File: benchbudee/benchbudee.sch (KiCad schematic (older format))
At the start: 0 parts

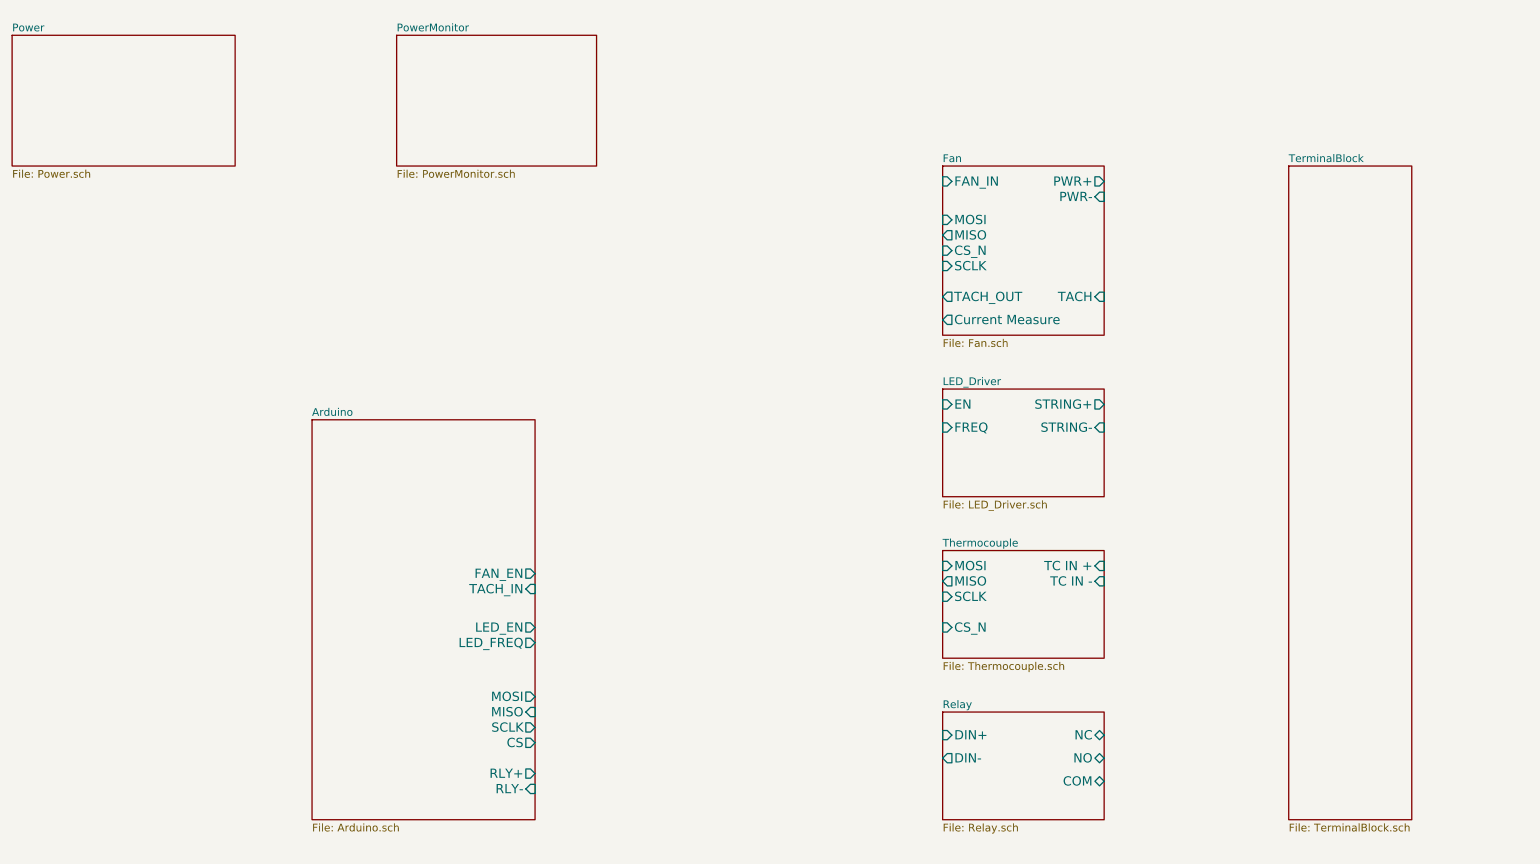
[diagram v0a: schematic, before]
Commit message: Added power monitor module
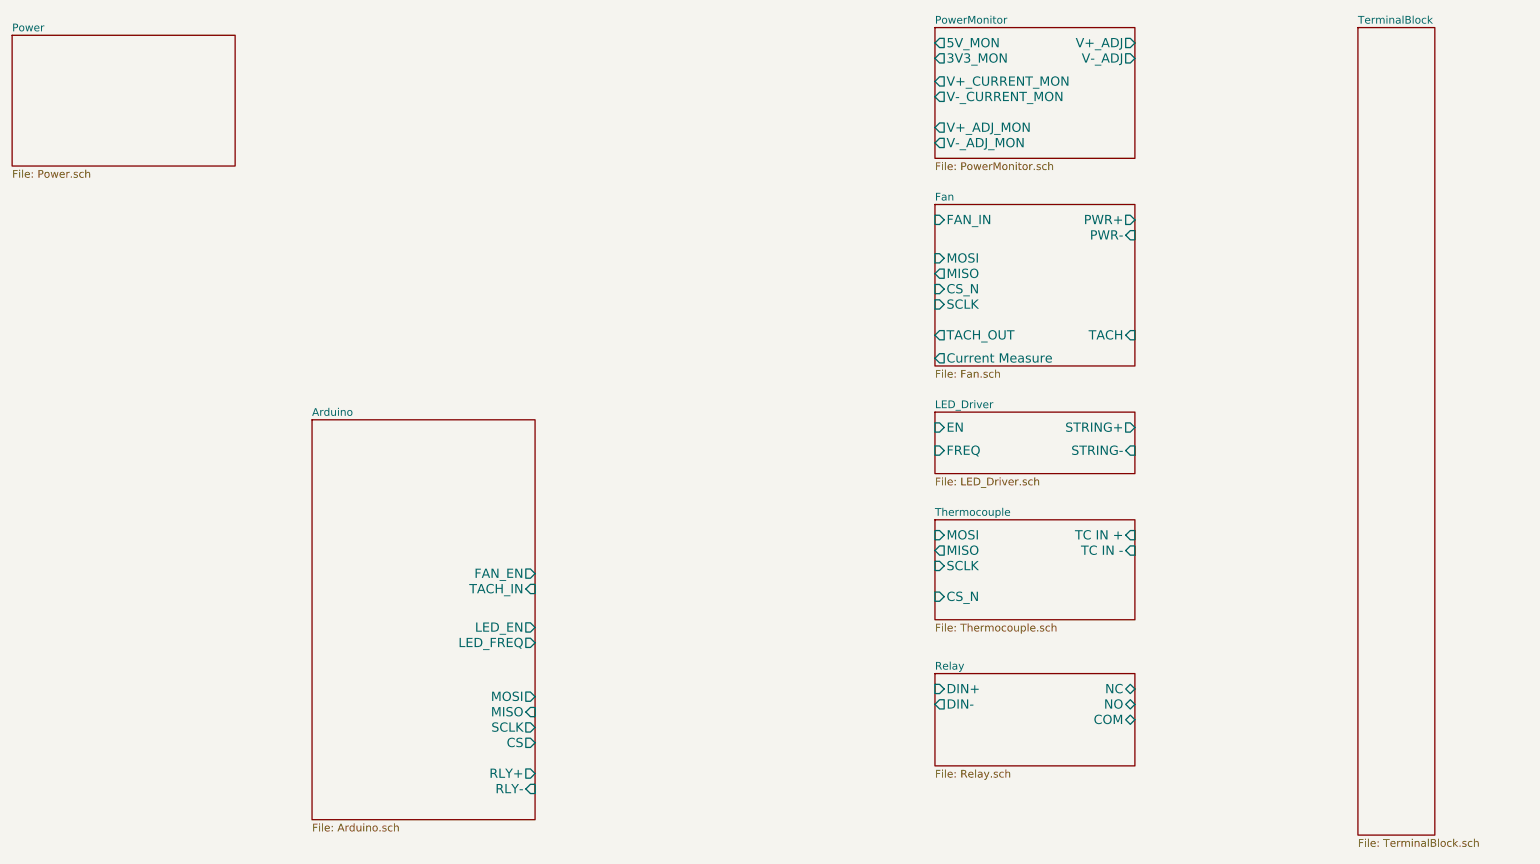
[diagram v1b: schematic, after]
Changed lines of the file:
@@
 Sheet 1 9
 Title ""
-Date "13 feb 2014"
+Date "14 feb 2014"
 Rev ""
 Comp ""
@@
 $EndSheet
 $Sheet
-S 7150 4300 1050 700
+S 7100 4100 1300 650
 U 52F13E8B
 F0 "Thermocouple" 50
 F1 "Thermocouple.sch" 50
-F2 "TC IN +" I R 8200 4400 60
-F3 "TC IN -" I R 8200 4500 60
-F4 "MOSI" I L 7150 4400 60
-F5 "MISO" O L 7150 4500 60
-F6 "SCLK" I L 7150 4600 60
-F7 "CS_N" I L 7150 4800 60
+F2 "TC IN +" I R 8400 4200 60
+F3 "TC IN -" I R 8400 4300 60
+F4 "MOSI" I L 7100 4200 60
+F5 "MISO" O L 7100 4300 60
+F6 "SCLK" I L 7100 4400 60
+F7 "CS_N" I L 7100 4600 60
 $EndSheet
 $Sheet
-S 7150 5350 1050 700
+S 7100 5100 1300 600
 U 52F13E9E
 F0 "Relay" 50
 F1 "Relay.sch" 50
-F2 "DIN+" I L 7150 5500 60
-F3 "DIN-" O L 7150 5650 60
-F4 "NC" B R 8200 5500 60
-F5 "NO" B R 8200 5650 60
-F6 "COM" B R 8200 5800 60
+F2 "DIN+" I L 7100 5200 60
+F3 "DIN-" O L 7100 5300 60
+F4 "NC" B R 8400 5200 60
+F5 "NO" B R 8400 5300 60
+F6 "COM" B R 8400 5400 60
 $EndSheet
 $Sheet
@@
 $EndSheet
 $Sheet
-S 7150 3250 1050 700
+S 7100 3400 1300 400
 U 52F1408A
 F0 "LED_Driver" 50
 F1 "LED_Driver.sch" 50
-F2 "EN" I L 7150 3350 60
-F3 "FREQ" I L 7150 3500 60
-F4 "STRING+" O R 8200 3350 60
-F5 "STRING-" I R 8200 3500 60
+F2 "EN" I L 7100 3500 60
+F3 "FREQ" I L 7100 3650 60
+F4 "STRING+" O R 8400 3500 60
+F5 "STRING-" I R 8400 3650 60
 $EndSheet
 $Sheet
-S 9400 1800 800  4250
+S 9850 900  500  5250
 U 52F140D2
 F0 "TerminalBlock" 50
@@
 $EndSheet
 $Sheet
-S 7150 1800 1050 1100
+S 7100 2050 1300 1050
 U 52F140AA
 F0 "Fan" 50
 F1 "Fan.sch" 50
-F2 "PWR+" O R 8200 1900 60
-F3 "PWR-" I R 8200 2000 60
-F4 "TACH" I R 8200 2650 60
-F5 "TACH_OUT" O L 7150 2650 60
-F6 "FAN_IN" I L 7150 1900 60
-F7 "Current Measure" O L 7150 2800 60
-F8 "MOSI" I L 7150 2150 60
-F9 "MISO" O L 7150 2250 60
-F10 "CS_N" I L 7150 2350 60
-F11 "SCLK" I L 7150 2450 60
+F2 "PWR+" O R 8400 2150 60
+F3 "PWR-" I R 8400 2250 60
+F4 "TACH" I R 8400 2900 60
+F5 "TACH_OUT" O L 7100 2900 60
+F6 "FAN_IN" I L 7100 2150 60
+F7 "Current Measure" O L 7100 3050 60
+F8 "MOSI" I L 7100 2400 60
+F9 "MISO" O L 7100 2500 60
+F10 "CS_N" I L 7100 2600 60
+F11 "SCLK" I L 7100 2700 60
 $EndSheet
 $Sheet
-S 3600 950  1300 850
+S 7100 900  1300 850
 U 52FC1BE1
 F0 "PowerMonitor" 50
 F1 "PowerMonitor.sch" 50
+F2 "V+_ADJ" O R 8400 1000 60
+F3 "V-_ADJ" O R 8400 1100 60
+F4 "3V3_MON" O L 7100 1100 60
+F5 "5V_MON" O L 7100 1000 60
+F6 "V+_ADJ_MON" O L 7100 1550 60
+F7 "V-_ADJ_MON" O L 7100 1650 60
+F8 "V+_CURRENT_MON" O L 7100 1250 60
+F9 "V-_CURRENT_MON" O L 7100 1350 60
 $EndSheet
 $EndSCHEMATC

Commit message: Added LED driver.
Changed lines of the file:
@@
 F0 "LED_Driver" 50
 F1 "LED_Driver.sch" 50
-F2 "EN" I L 7100 3500 60
-F3 "FREQ" I L 7100 3650 60
-F4 "STRING+" O R 8400 3500 60
-F5 "STRING-" I R 8400 3650 60
+F2 "STRING+" O R 8400 3500 60
+F3 "STRING-" I R 8400 3650 60
+F4 "LED_EN_PWM" I L 7100 3500 60
 $EndSheet
 $Sheet

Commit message: Setting up for layout
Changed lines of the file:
@@
 LIBS:benchbudee-custom
 LIBS:benchbudee-cache
-EELAYER 27 0
+EELAYER 24 0
 EELAYER END
 $Descr A4 11693 8268
@@
 $EndDescr
 $Sheet
-S 3050 3450 1450 2600
-U 52F13E2E
-F0 "Arduino" 50
-F1 "Arduino.sch" 50
-F2 "RLY+" O R 4500 5750 60
-F3 "RLY-" I R 4500 5850 60
-F4 "MOSI" O R 4500 5250 60
-F5 "MISO" I R 4500 5350 60
-F6 "SCLK" O R 4500 5450 60
-F7 "CS" O R 4500 5550 60
-F8 "LED_EN" O R 4500 4800 60
-F9 "LED_FREQ" O R 4500 4900 60
-F10 "FAN_EN" O R 4500 4450 60
-F11 "TACH_IN" I R 4500 4550 60
-$EndSheet
-$Sheet
-S 7100 4100 1300 650
+S 6250 3500 1450 650
 U 52F13E8B
 F0 "Thermocouple" 50
 F1 "Thermocouple.sch" 50
-F2 "TC IN +" I R 8400 4200 60
-F3 "TC IN -" I R 8400 4300 60
-F4 "MOSI" I L 7100 4200 60
-F5 "MISO" O L 7100 4300 60
-F6 "SCLK" I L 7100 4400 60
-F7 "CS_N" I L 7100 4600 60
-$EndSheet
-$Sheet
-S 7100 5100 1300 600
+F2 "TC IN +" I R 7700 3600 60
+F3 "TC IN -" I R 7700 3700 60
+F4 "MOSI" I L 6250 3600 60
+F5 "MISO" O L 6250 3700 60
+F6 "SCLK" I L 6250 3800 60
+F7 "CS_N" I L 6250 3900 60
+$EndSheet
+$Sheet
+S 6250 5300 1450 550
 U 52F13E9E
 F0 "Relay" 50
 F1 "Relay.sch" 50
-F2 "DIN+" I L 7100 5200 60
-F3 "DIN-" O L 7100 5300 60
-F4 "NC" B R 8400 5200 60
-F5 "NO" B R 8400 5300 60
-F6 "COM" B R 8400 5400 60
+F2 "RELAY_NC" B R 7700 5400 60
+F3 "RELAY_NO" B R 7700 5500 60
+F4 "RELAY_COM" B R 7700 5600 60
+F5 "RELAY+" I L 6250 5400 60
+F6 "RELAY-" O L 6250 5500 60
 $EndSheet
 $Sheet
@@
 $EndSheet
 $Sheet
-S 7100 3400 1300 400
+S 6250 4450 1450 450
 U 52F1408A
 F0 "LED_Driver" 50
 F1 "LED_Driver.sch" 50
-F2 "STRING+" O R 8400 3500 60
-F3 "STRING-" I R 8400 3650 60
-F4 "LED_EN_PWM" I L 7100 3500 60
-$EndSheet
-$Sheet
-S 9850 900  500  5250
+F2 "LED_EN_PWM" I L 6250 4550 60
+F3 "LED_STRING+" O R 7700 4550 60
+F4 "LED_STRING-" O R 7700 4700 60
+$EndSheet
+$Sheet
+S 6250 1100 1450 900
+U 52FC1BE1
+F0 "PowerMonitor" 50
+F1 "PowerMonitor.sch" 50
+F2 "V+_ADJ" O R 7700 1200 60
+F3 "V-_ADJ" O R 7700 1350 60
+F4 "3V3_MON" O L 6250 1300 60
+F5 "5V_MON" O L 6250 1200 60
+F6 "V+_ADJ_MON" O L 6250 1750 60
+F7 "V-_ADJ_MON" O L 6250 1850 60
+F8 "V+_CURRENT_MON" O L 6250 1450 60
+F9 "V-_CURRENT_MON" O L 6250 1550 60
+$EndSheet
+Wire Wire Line
+	7700 1200 7700 1250
+Wire Wire Line
+	7700 1250 9000 1250
+Wire Wire Line
+	7700 1350 9000 1350
+Wire Wire Line
+	7700 2350 9050 2350
+Wire Wire Line
+	7700 2500 9000 2500
+Wire Wire Line
+	7700 3100 9000 3100
+Wire Wire Line
+	7700 5400 9000 5400
+Wire Wire Line
+	7700 5500 9000 5500
+Wire Wire Line
+	7700 5600 9000 5600
+Wire Wire Line
+	4750 3000 4900 3000
+Wire Wire Line
+	4900 3000 4900 1750
+Wire Wire Line
+	4900 1750 6250 1750
+Wire Wire Line
+	4750 3100 5000 3100
+Wire Wire Line
+	5000 3100 5000 1850
+Wire Wire Line
+	5000 1850 6250 1850
+Wire Wire Line
+	4750 3450 5250 3450
+Wire Wire Line
+	5250 3450 5250 2450
+Wire Wire Line
+	5250 2450 6250 2450
+Wire Wire Line
+	4750 3600 5300 3600
+Wire Wire Line
+	5300 3600 6250 3600
+Wire Wire Line
+	5300 3600 5300 2650
+Wire Wire Line
+	5300 2650 6250 2650
+Wire Wire Line
+	4750 3700 5350 3700
+Wire Wire Line
+	5350 3700 6250 3700
+Wire Wire Line
+	5350 3700 5350 2750
+Wire Wire Line
+	5350 2750 6250 2750
+Wire Wire Line
+	5400 3800 5400 2850
+Wire Wire Line
+	5400 2850 6250 2850
+Wire Wire Line
+	4750 4050 5500 4050
+Wire Wire Line
+	5500 4050 5500 3100
+Wire Wire Line
+	5500 3100 6250 3100
+Wire Wire Line
+	4750 4150 5550 4150
+Wire Wire Line
+	5550 4150 5550 3200
+Wire Wire Line
+	5550 3200 6250 3200
+Wire Wire Line
+	4750 4550 6250 4550
+$Sheet
+S 9000 1100 1250 4750
 U 52F140D2
 F0 "TerminalBlock" 50
 F1 "TerminalBlock.sch" 50
-$EndSheet
-$Sheet
-S 7100 2050 1300 1050
+F2 "V+_ADJ" I L 9000 1250 60
+F3 "V-_ADJ" I L 9000 1350 60
+F4 "FAN_OUT+" O L 9000 2350 60
+F5 "FAN_OUT-" O L 9000 2500 60
+F6 "TACH_IN" O L 9000 3100 60
+F7 "LED_STRING+" O L 9000 4550 60
+F8 "LED_STRING-" O L 9000 4700 60
+F9 "TC_IN+" I L 9000 3600 60
+F10 "TC_IN-" I L 9000 3700 60
+F11 "RELAY_NO" B L 9000 5500 60
+F12 "RELAY_NC" B L 9000 5400 60
+F13 "RELAY_COM" B L 9000 5600 60
+$EndSheet
+Wire Wire Line
+	7700 3600 9000 3600
+Wire Wire Line
+	7700 3700 9000 3700
+Wire Wire Line
+	7700 4550 9000 4550
+Wire Wire Line
+	7700 4700 9000 4700
+Connection ~ 5300 3600
+Connection ~ 5350 3700
+Wire Wire Line
+	4750 3800 5400 3800
+Wire Wire Line
+	5400 3800 6250 3800
+Connection ~ 5400 3800
+Wire Wire Line
+	4750 3900 5450 3900
+Wire Wire Line
+	5450 3900 5450 2950
+Wire Wire Line
+	5450 2950 6250 2950
+Wire Wire Line
+	4750 4350 5750 4350
+Wire Wire Line
+	5750 4350 5750 3900
+Wire Wire Line
+	5750 3900 6250 3900
+Wire Wire Line
+	4750 5400 6250 5400
+Wire Wire Line
+	6250 5500 4750 5500
+Wire Wire Line
+	4750 3350 5200 3350
+Wire Wire Line
+	5200 3350 5200 2350
+Wire Wire Line
+	5200 2350 6250 2350
+$Sheet
+S 6250 2250 1450 1000
 U 52F140AA
 F0 "Fan" 50
 F1 "Fan.sch" 50
-F2 "PWR+" O R 8400 2150 60
-F3 "PWR-" I R 8400 2250 60
-F4 "TACH" I R 8400 2900 60
-F5 "TACH_OUT" O L 7100 2900 60
-F6 "FAN_IN" I L 7100 2150 60
-F7 "Current Measure" O L 7100 3050 60
-F8 "MOSI" I L 7100 2400 60
-F9 "MISO" O L 7100 2500 60
-F10 "CS_N" I L 7100 2600 60
-F11 "SCLK" I L 7100 2700 60
-$EndSheet
-$Sheet
-S 7100 900  1300 850
-U 52FC1BE1
-F0 "PowerMonitor" 50
-F1 "PowerMonitor.sch" 50
-F2 "V+_ADJ" O R 8400 1000 60
-F3 "V-_ADJ" O R 8400 1100 60
-F4 "3V3_MON" O L 7100 1100 60
-F5 "5V_MON" O L 7100 1000 60
-F6 "V+_ADJ_MON" O L 7100 1550 60
-F7 "V-_ADJ_MON" O L 7100 1650 60
-F8 "V+_CURRENT_MON" O L 7100 1250 60
-F9 "V-_CURRENT_MON" O L 7100 1350 60
+F2 "MOSI" I L 6250 2650 60
+F3 "MISO" O L 6250 2750 60
+F4 "CS_N" I L 6250 2950 60
+F5 "SCLK" I L 6250 2850 60
+F6 "FAN_OUT+" O R 7700 2350 60
+F7 "FAN_OUT-" O R 7700 2500 60
+F8 "TACH_IN" I R 7700 3100 60
+F9 "TACH_MEAS" O L 6250 3100 60
+F10 "CURR_MEAS" O L 6250 3200 60
+F11 "FAN_PWM" I L 6250 2450 60
+F12 "FAN_MODE" I L 6250 2350 60
+$EndSheet
+$Sheet
+S 3350 2900 1400 2750
+U 52F13E2E
+F0 "Arduino" 50
+F1 "Arduino.sch" 50
+F2 "MOSI" O R 4750 3600 60
+F3 "MISO" I R 4750 3700 60
+F4 "SCLK" O R 4750 3800 60
+F5 "RELAY-" O R 4750 5500 60
+F6 "RELAY+" O R 4750 5400 60
+F7 "TACH_MEAS" I R 4750 4050 60
+F8 "CURR_MEAS" I R 4750 4150 60
+F9 "V+_ADJ_MON" I R 4750 3000 60
+F10 "V-_ADJ_MON" I R 4750 3100 60
+F11 "LED_EN_PWM" O R 4750 4550 60
+F12 "FAN_CS_N" O R 4750 3900 60
+F13 "TC_CS_N" O R 4750 4350 60
+F14 "FAN_PWM" O R 4750 3450 60
+F15 "FAN_MODE" O R 4750 3350 60
 $EndSheet
 $EndSCHEMATC

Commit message: Relay module footprints done
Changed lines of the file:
@@
 	5250 2450 6250 2450
 Wire Wire Line
-	4750 3600 5300 3600
-Wire Wire Line
-	5300 3600 6250 3600
+	4750 3600 6250 3600
 Wire Wire Line
 	5300 3600 5300 2650
@@
 	5300 2650 6250 2650
 Wire Wire Line
-	4750 3700 5350 3700
-Wire Wire Line
-	5350 3700 6250 3700
+	4750 3700 6250 3700
 Wire Wire Line
 	5350 3700 5350 2750
@@
 Connection ~ 5350 3700
 Wire Wire Line
-	4750 3800 5400 3800
-Wire Wire Line
-	5400 3800 6250 3800
+	4750 3800 6250 3800
 Connection ~ 5400 3800
 Wire Wire Line
